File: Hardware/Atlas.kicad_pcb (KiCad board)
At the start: 2 copper layers, 80.5 x 70 mm, 49 parts, among them J1 DC, U1 MS5611, U2 HTU21D, U3 uSD Card, U4 RFD900, U5 MPU9150, U6 XBEE, U7 VENUS838FLPX-L, U8 AOZ1031

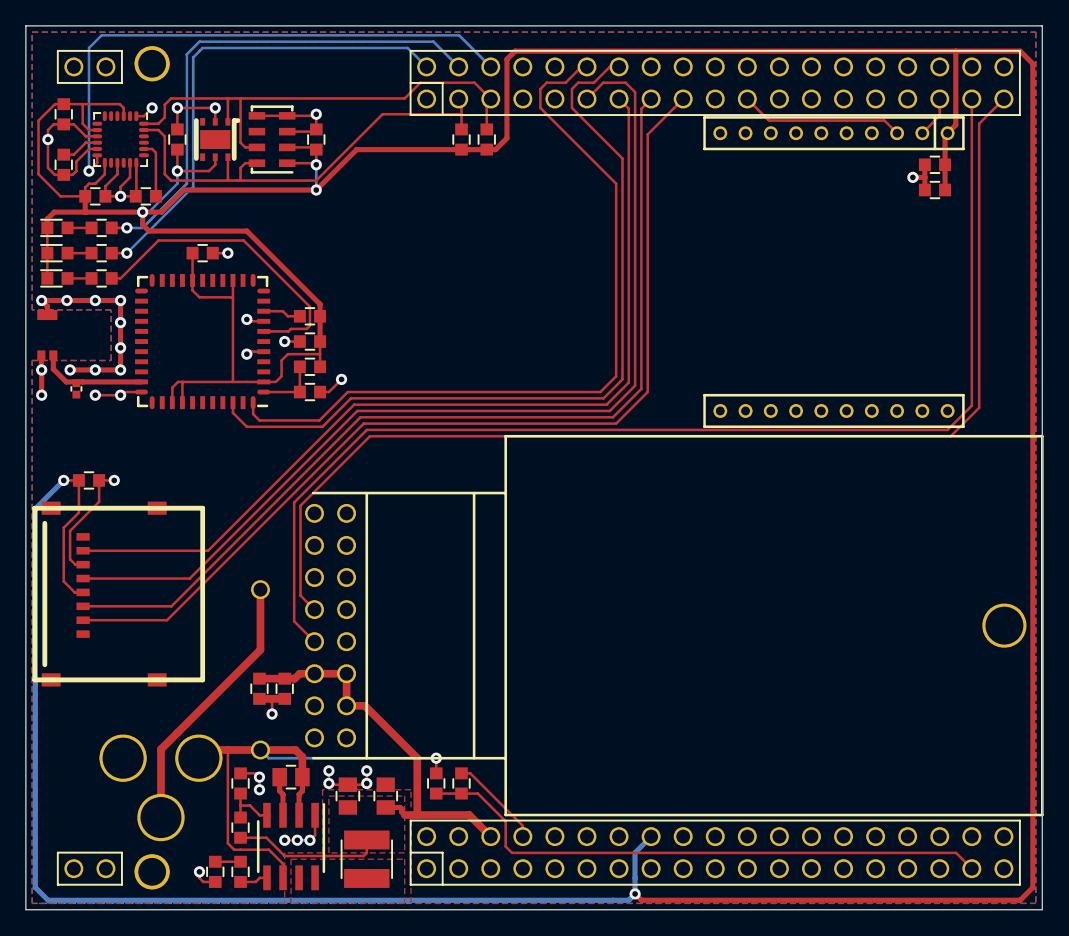
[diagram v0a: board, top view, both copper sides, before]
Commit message: Add isolation routing and ground stitching
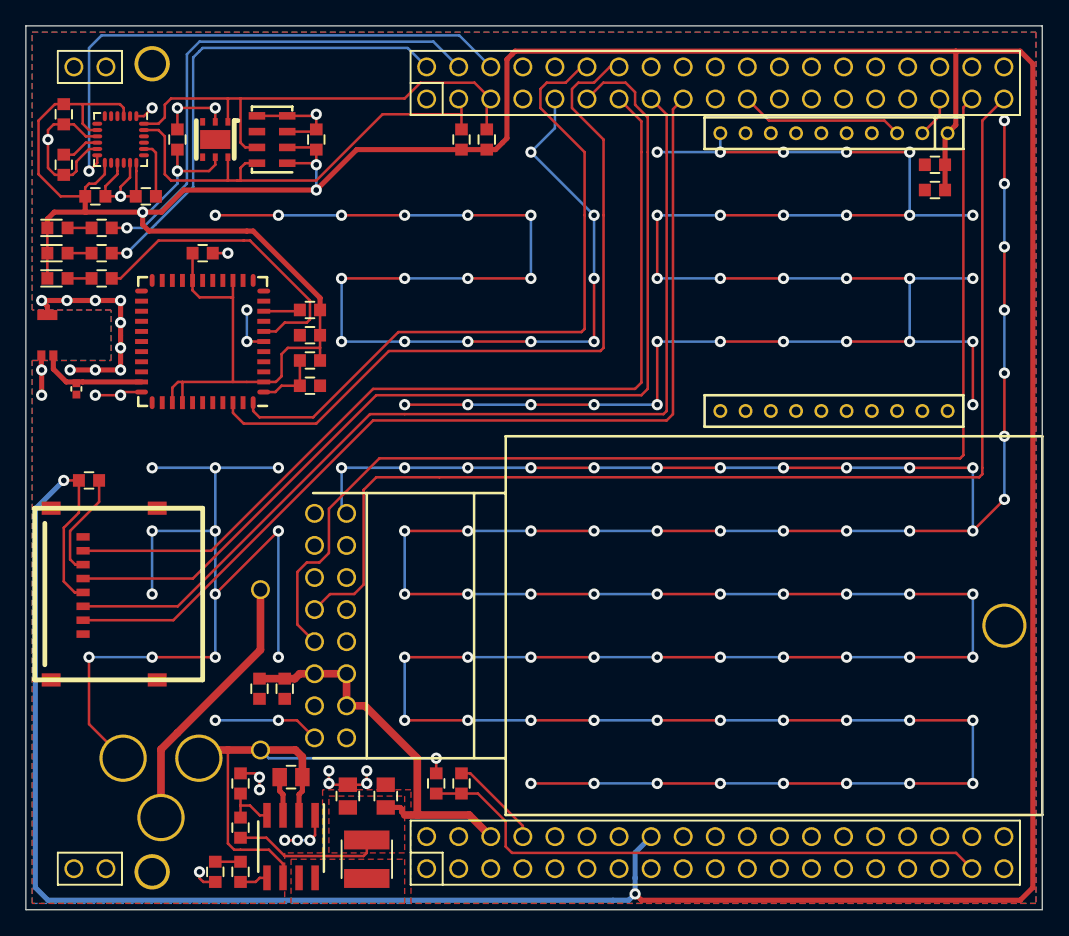
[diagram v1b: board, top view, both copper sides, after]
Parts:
- moved C12 0.50 mm to (122.5, 98.5)
- moved C13 0.50 mm to (122.5, 94.5)
- moved R1 0.50 mm to (122.5, 96.5)
- moved R12 0.50 mm to (122.5, 92.5)
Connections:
- MECH-HOLE220 pad : (no net) -> GND (x2)
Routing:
- net GND: track 111.0 -> 741.9 mm, vias 37 -> 159
- net /GOMI: track 61.0 -> 54.9 mm
- net /GIMO: track 62.8 -> 59.0 mm
- net /MOSI: track 74.6 -> 77.8 mm
- net /CS: track 76.6 -> 78.8 mm
- net /SCK: track 77.9 -> 79.5 mm
- net /MISO: track 71.5 -> 72.9 mm
- net /LOMI: track 90.9 -> 92.1 mm

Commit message: Switch IMU to QFN footprint
Fixes #6
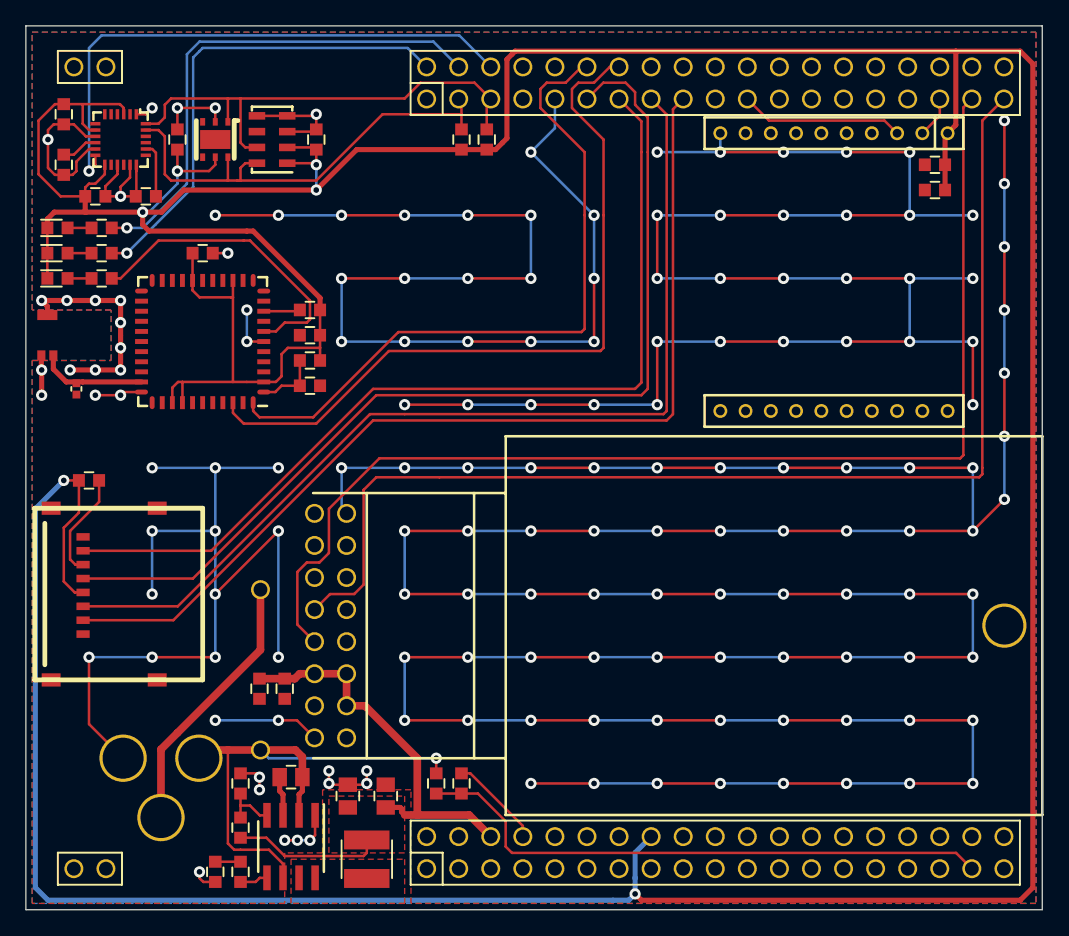
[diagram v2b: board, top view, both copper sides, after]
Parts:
- removed MECH-HOLE220 (x2): VAL**, MECH-HOLE220
- C16: value C -> 3300pF
- D1: value NAV -> RED
- D2: value LED -> GRN
- D3: value LED -> YLW
- L1: value L -> DNP
- R1: value 33k -> 30k
- R10, R11, R4: value R -> 75
- R5, R6: value R -> 30k
- R9: value R -> 10k
- U5: footprint PQFN50P400X400-24N -> QFN50P400X400-24N
- turned U5 to 180 degrees

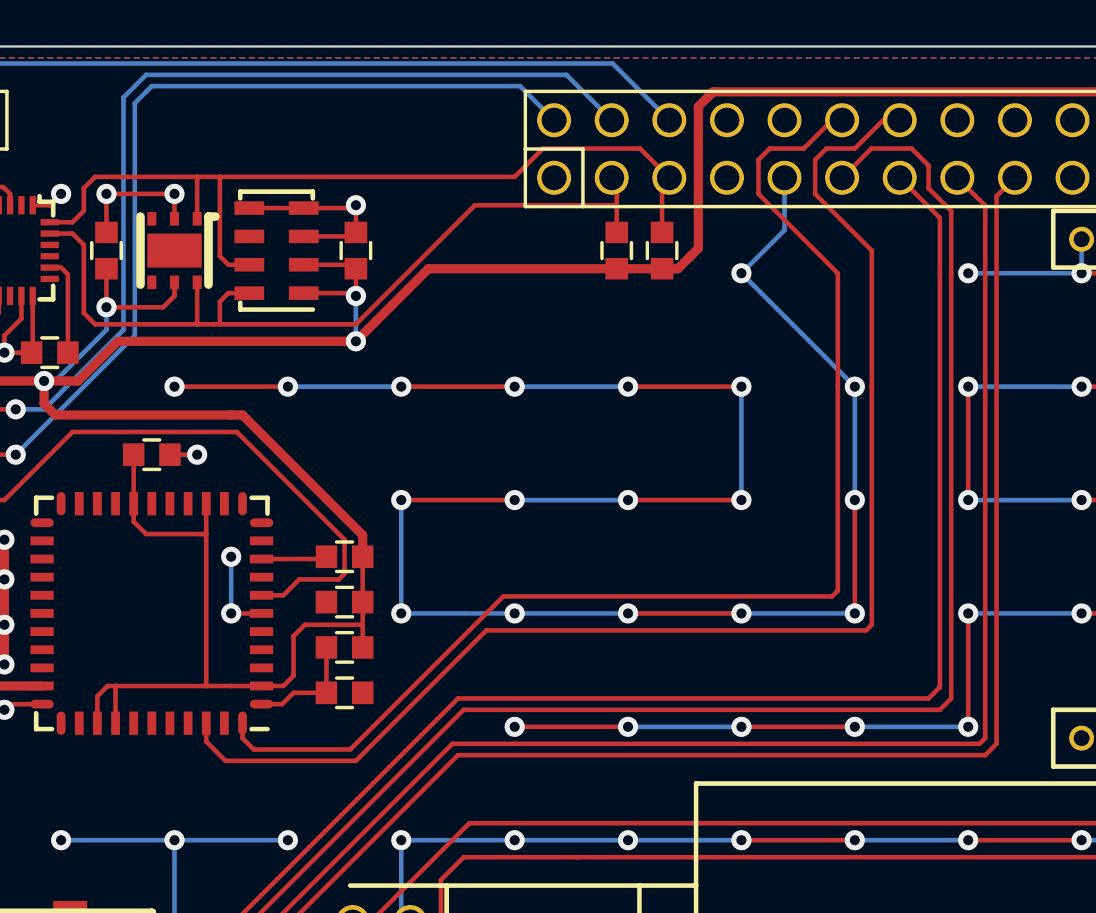
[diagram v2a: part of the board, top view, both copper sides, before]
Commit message: Connect GPS PPS output
Closes #5
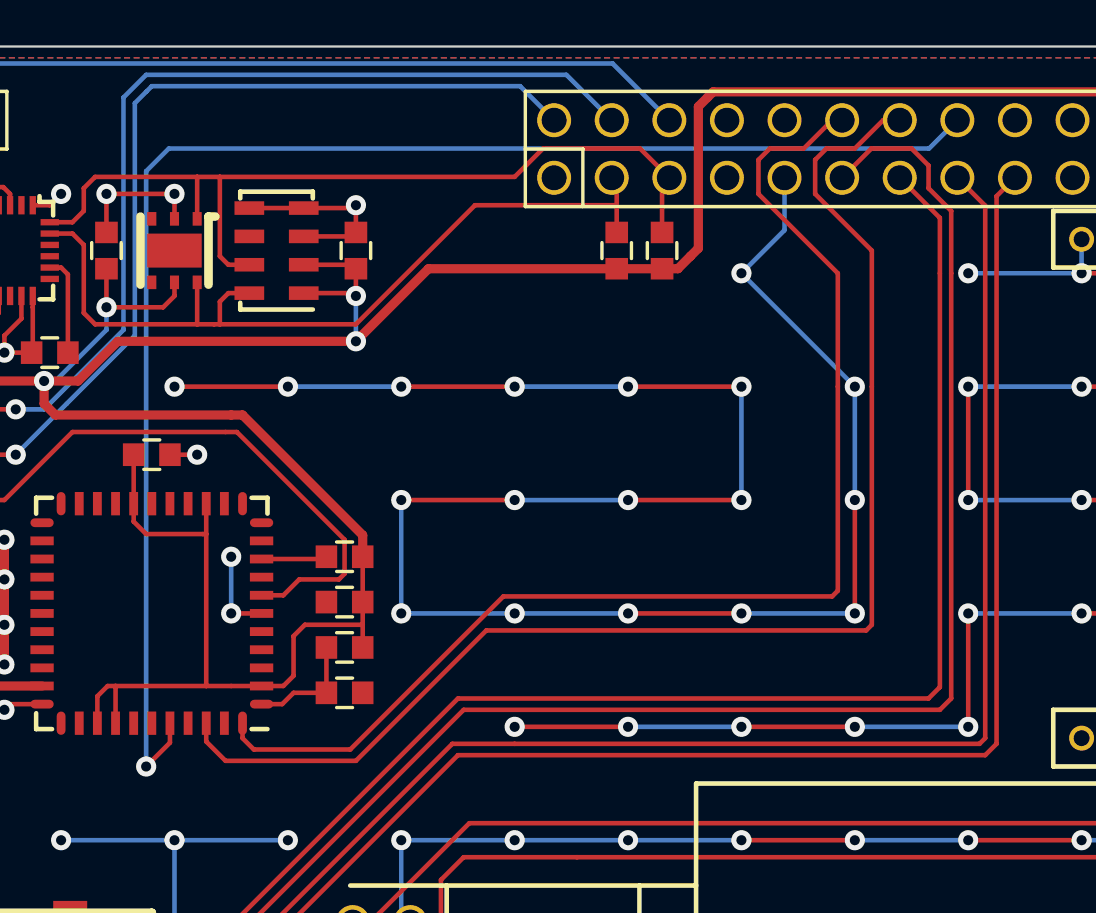
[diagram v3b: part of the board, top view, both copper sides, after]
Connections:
- H1 pad E16: (no net) -> /PPS
- U7 pad 40: (no net) -> /PPS
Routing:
- net /PPS: track 0.00 -> 65.3 mm, vias 0 -> 1

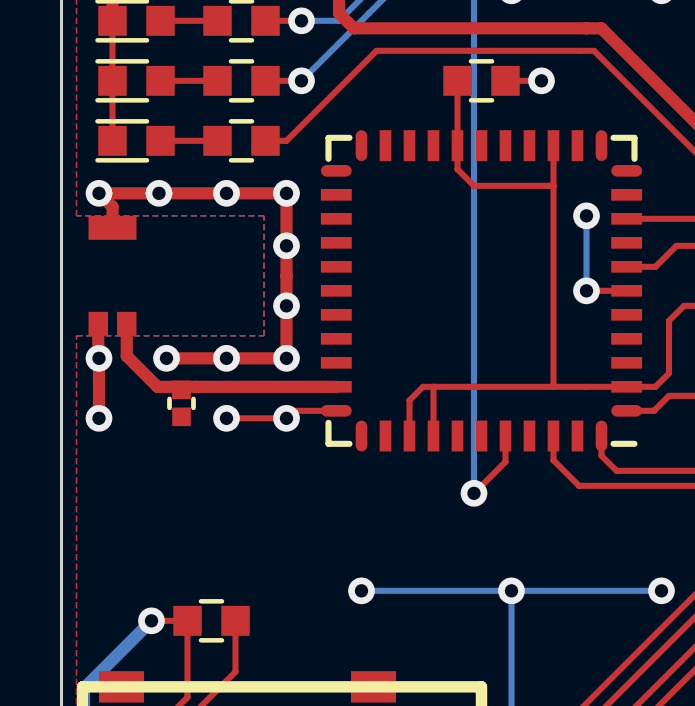
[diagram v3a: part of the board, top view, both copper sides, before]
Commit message: Switch GPS to SMA antennas port
Add pull up inductor to support active antenna. Closes #7
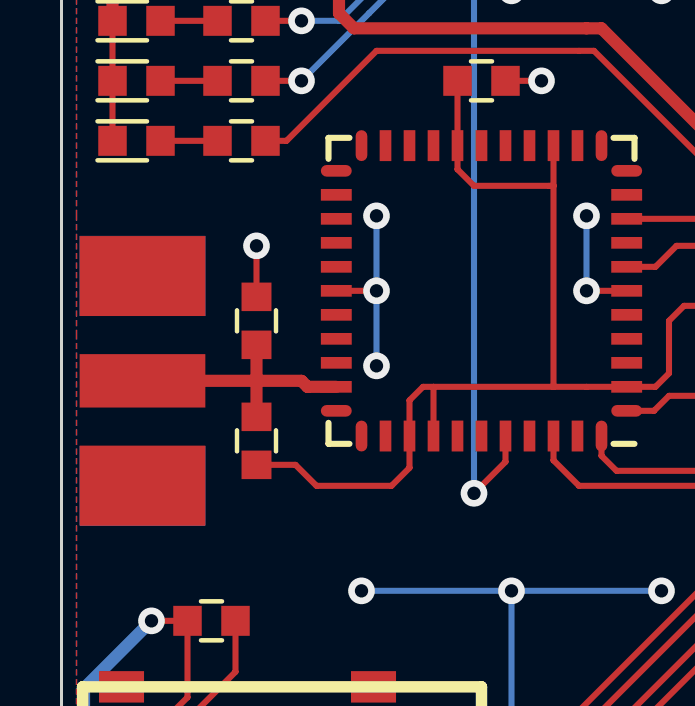
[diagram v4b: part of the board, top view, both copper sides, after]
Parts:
- added L3: L, INDC1608-N, F.Cu at (106.5, 100.0)
- AE1: footprint ANT-W3011A -> SMA_Edge
- L1: footprint INDC1005-N -> INDC1608-N
- moved L1 3.72 mm to (106.5, 96.0), turned to 270 degrees
- moved AE1 3.50 mm to (100.5, 98.0), turned to 0 degrees
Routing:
- net GND: track 741.8 -> 725.8 mm, vias 159 -> 150
- net +3.3V: track 395.3 -> 402.0 mm
